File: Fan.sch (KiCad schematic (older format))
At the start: 9 parts, among them Q2 MOSFET_N, Q3 MOSFET_N, Q4 MOSFET_N, U11 OPA4170, U8 MCP4922-E/P

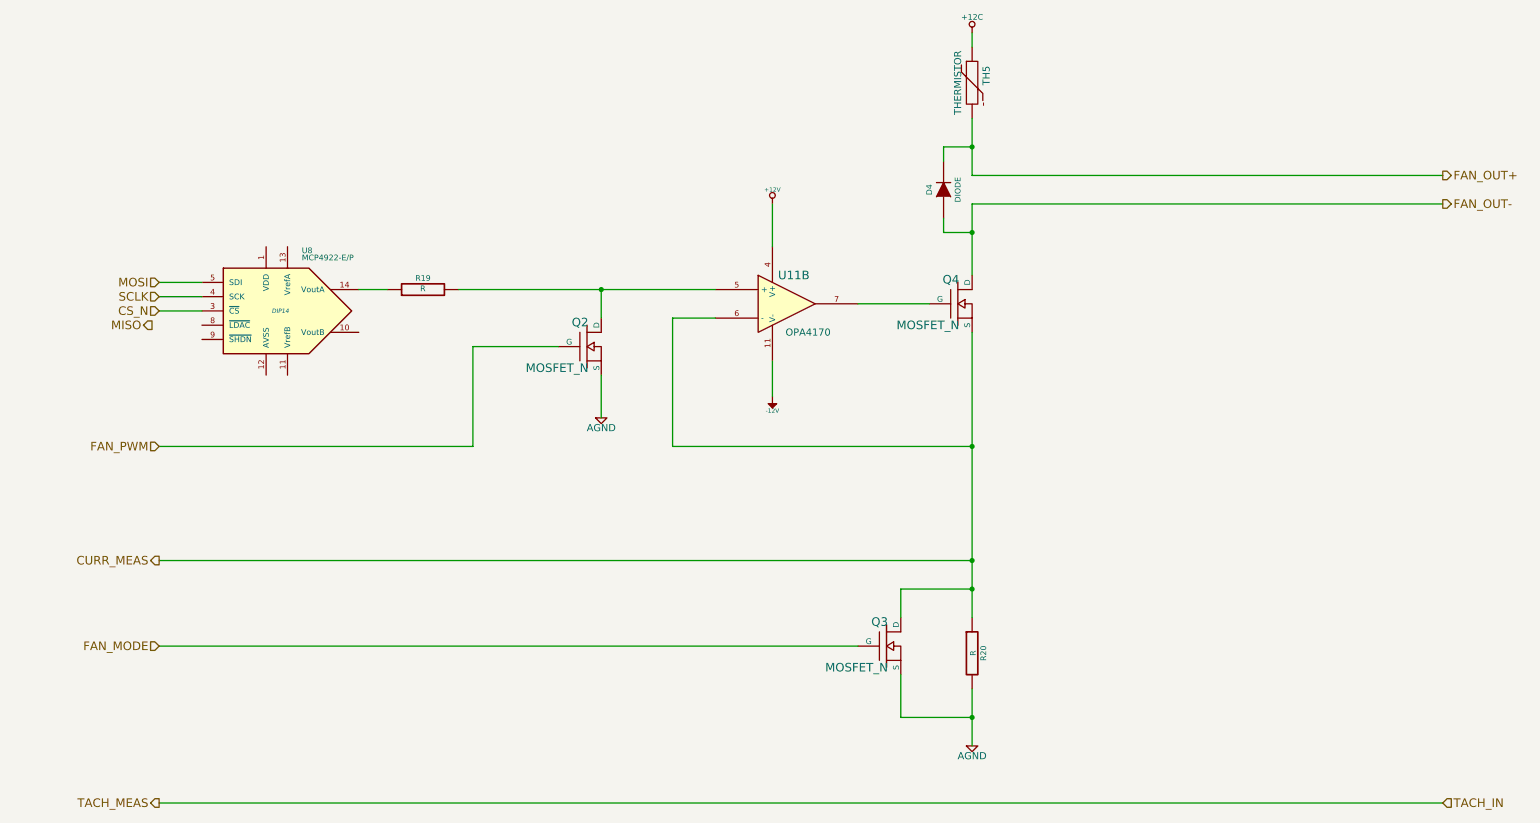
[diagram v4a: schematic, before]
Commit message: Associated and placed the Current/Fan Driver Module
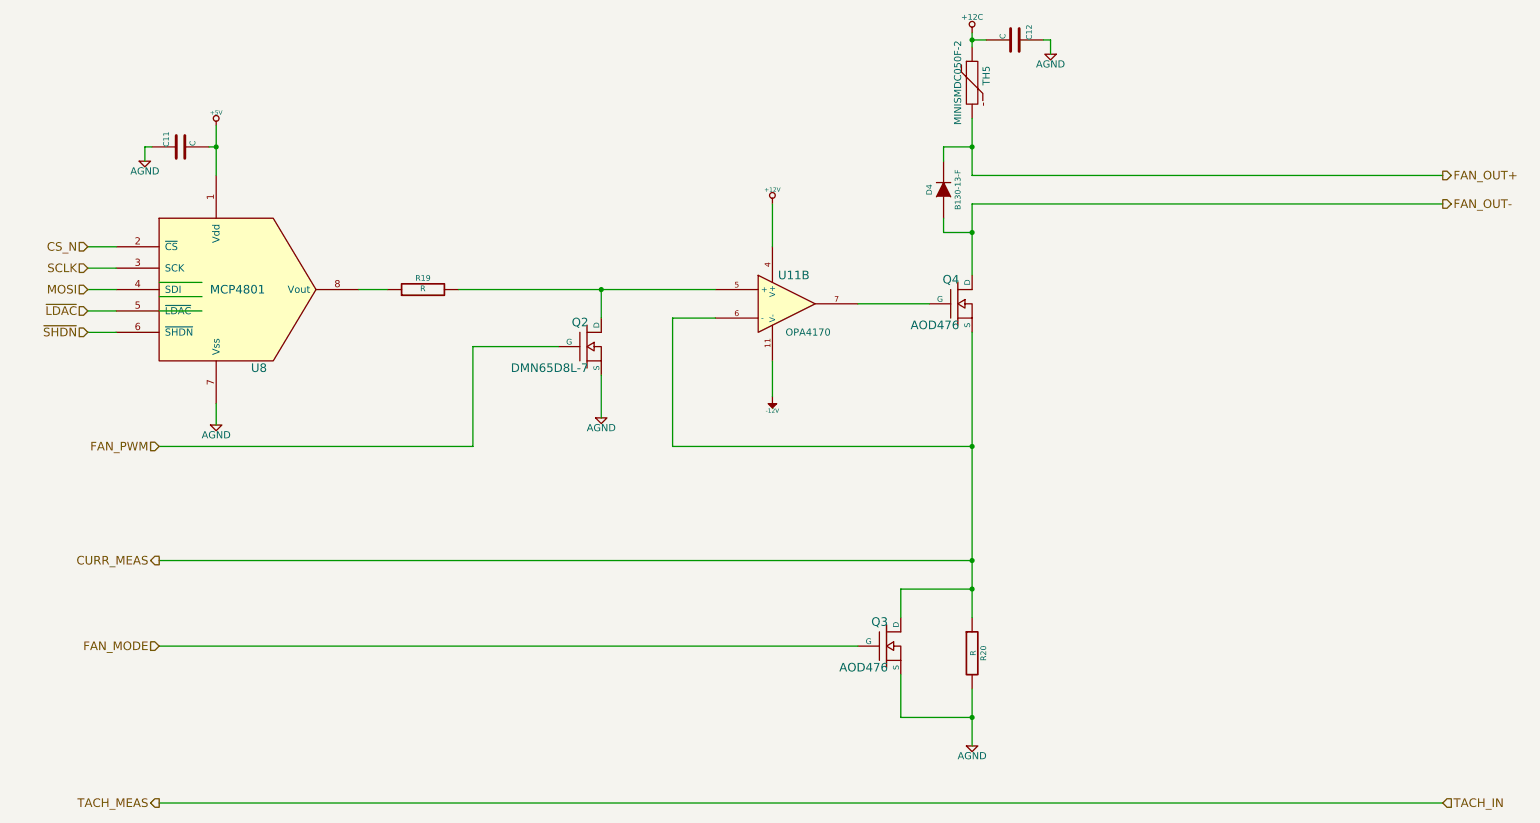
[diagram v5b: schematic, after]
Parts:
- removed Q2, Q3, Q4: MOSFET_N, symbol MOSFET_N
- removed U8: MCP4922-E/P, DIP14, symbol MCP4922-E/P
- added C11, C12: C, symbol C
- added Q2: DMN65D8L-7, symbol MOSFET_N_NUM
- added Q3, Q4: AOD476, symbol MOSFET_N_NUM
- added U8: MCP4801, symbol MCP4801
- D4: value DIODE -> B130-13-F; MFG Name (none) -> Diodes Inc; MFG Part Number (none) -> B130-13-F
- TH5: value THERMISTOR -> MINISMDC050F-2; MFG Name (none) -> TE; MFG Part Number (none) -> MINISMDC050F-2
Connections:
- net labels added: +5V, ~LDAC, ~SHDN
- net labels removed: MISO
- wire segments 34 -> 47
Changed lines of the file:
@@
-$EndComp
-$Comp
-L MOSFET_N Q4
-U 1 1 52F026F4
-P 7100 2600
-F 0 "Q4" H 7110 2770 60  0000 R CNN
-F 1 "MOSFET_N" H 7110 2450 60  0000 R CNN
-F 2 "" H 7100 2600 60  0000 C CNN
-F 3 "" H 7100 2600 60  0000 C CNN
-	1    7100 2600
-	1    0    0    -1
 $EndComp
 $Comp
@@
 $EndComp
 $Comp
-L AGND #PWR42
+L AGND #PWR45
 U 1 1 52F02747
 P 7200 5700
-F 0 "#PWR42" H 7200 5700 40  0001 C CNN
+F 0 "#PWR45" H 7200 5700 40  0001 C CNN
 F 1 "AGND" H 7200 5630 50  0000 C CNN
 F 2 "" H 7200 5700 60  0000 C CNN
@@
 $EndComp
 $Comp
-L +12V #PWR39
+L +12V #PWR42
 U 1 1 52F02768
 P 5800 1900
-F 0 "#PWR39" H 5800 1850 20  0001 C CNN
+F 0 "#PWR42" H 5800 1850 20  0001 C CNN
 F 1 "+12V" H 5800 2000 30  0000 C CNN
 F 2 "" H 5800 1900 60  0000 C CNN
@@
 $EndComp
 $Comp
-L -12V #PWR40
+L -12V #PWR43
 U 1 1 52F02786
 P 5800 3250
-F 0 "#PWR40" H 5800 3380 20  0001 C CNN
+F 0 "#PWR43" H 5800 3380 20  0001 C CNN
 F 1 "-12V" H 5800 3350 30  0000 C CNN
 F 2 "" H 5800 3250 60  0000 C CNN
@@
 $EndComp
 $Comp
-L AGND #PWR38
+L AGND #PWR41
 U 1 1 52F0282F
 P 4600 3400
-F 0 "#PWR38" H 4600 3400 40  0001 C CNN
+F 0 "#PWR41" H 4600 3400 40  0001 C CNN
 F 1 "AGND" H 4600 3330 50  0000 C CNN
 F 2 "" H 4600 3400 60  0000 C CNN
 F 3 "" H 4600 3400 60  0000 C CNN
 	1    4600 3400
-	1    0    0    -1
-$EndComp
-$Comp
-L MCP4922-E/P U8
-U 1 1 52F0284E
-P 2350 2650
-F 0 "U8" H 2500 3050 40  0000 L BNN
-F 1 "MCP4922-E/P" H 2500 3000 40  0000 L BNN
-F 2 "DIP14" H 2350 2650 30  0000 C CIN
-F 3 "" H 2350 2650 60  0000 C CNN
-	1    2350 2650
 	1    0    0    -1
 $EndComp
@@
 	0    -1   -1   0
 $EndComp
-Text HLabel 1500 2450 0    60   Input ~ 0
+Text HLabel 1000 2500 0    60   Input ~ 0
 MOSI
-Text HLabel 1450 2750 0    60   Output ~ 0
-MISO
-Text HLabel 1500 2650 0    60   Input ~ 0
+Text HLabel 1000 2200 0    60   Input ~ 0
 CS_N
-Text HLabel 1500 2550 0    60   Input ~ 0
+Text HLabel 1000 2350 0    60   Input ~ 0
 SCLK
-$Comp
-L MOSFET_N Q3
-U 1 1 52FBE00D
-P 6600 5000
-F 0 "Q3" H 6610 5170 60  0000 R CNN
-F 1 "MOSFET_N" H 6610 4850 60  0000 R CNN
-F 2 "" H 6600 5000 60  0000 C CNN
-F 3 "" H 6600 5000 60  0000 C CNN
-	1    6600 5000
-	1    0    0    -1
-$EndComp
 $Comp
 L THERMISTOR TH5
@@
 P 7200 1050
 F 0 "TH5" V 7300 1100 50  0000 C CNN
-F 1 "THERMISTOR" V 7100 1050 50  0000 C CNN
+F 1 "MINISMDC050F-2" V 7100 1050 50  0000 C CNN
 F 2 "" H 7200 1050 60  0000 C CNN
 F 3 "" H 7200 1050 60  0000 C CNN
+F 4 "TE" H 7200 1050 60  0001 C CNN "MFG Name"
+F 5 "MINISMDC050F-2" H 7200 1050 60  0001 C CNN "MFG Part Number"
 	1    7200 1050
 	1    0    0    -1
@@
 P 7000 1800
 F 0 "D4" H 7000 1900 40  0000 C CNN
-F 1 "DIODE" H 7000 1700 40  0000 C CNN
+F 1 "B130-13-F" H 7000 1700 40  0000 C CNN
 F 2 "" H 7000 1800 60  0000 C CNN
 F 3 "" H 7000 1800 60  0000 C CNN
+F 4 "Diodes Inc" H 7000 1800 60  0001 C CNN "MFG Name"
+F 5 "B130-13-F" H 7000 1800 60  0001 C CNN "MFG Part Number"
 	1    7000 1800
 	0    -1   -1   0
@@
 Wire Wire Line
 	10500 6100 1500 6100
-$Comp
-L MOSFET_N Q2
-U 1 1 52FBE558
-P 4500 2900
-F 0 "Q2" H 4510 3070 60  0000 R CNN
-F 1 "MOSFET_N" H 4510 2750 60  0000 R CNN
-F 2 "" H 4500 2900 60  0000 C CNN
-F 3 "" H 4500 2900 60  0000 C CNN
-	1    4500 2900
-	1    0    0    -1
-$EndComp
 Wire Wire Line
 	4600 2700 4600 2500
@@
 	1500 5000 6400 5000
 $Comp
-L +12C #PWR41
+L +12C #PWR44
 U 1 1 52FBEABF
 P 7200 700
-F 0 "#PWR41" H 7200 670 30  0001 C CNN
+F 0 "#PWR44" H 7200 670 30  0001 C CNN
 F 1 "+12C" H 7200 810 40  0000 C CNN
 F 2 "" H 7200 700 60  0000 C CNN
@@
 	1    0    0    -1
 $EndComp
+$Comp
+L MCP4801 U8
+U 1 1 53090AC6
+P 1900 2500
+F 0 "U8" H 2200 1950 60  0000 C CNN
+F 1 "MCP4801" H 2050 2500 60  0000 C CNN
+F 2 "" H 1900 2500 60  0000 C CNN
+F 3 "" H 1900 2500 60  0000 C CNN
+	1    1900 2500
+	1    0    0    -1
+$EndComp
+Wire Wire Line
+	1000 2200 1200 2200
+Wire Wire Line
+	1000 2350 1200 2350
+Wire Wire Line
+	1000 2500 1200 2500
+Text HLabel 1000 2650 0    60   Input ~ 0
+~LDAC
+Text HLabel 1000 2800 0    60   Input ~ 0
+~SHDN
+Wire Wire Line
+	1000 2650 1200 2650
+Wire Wire Line
+	1000 2800 1200 2800
+$Comp
+L +5V #PWR39
+U 1 1 530AC1D4
+P 1900 1350
+F 0 "#PWR39" H 1900 1440 20  0001 C CNN
+F 1 "+5V" H 1900 1440 30  0000 C CNN
+F 2 "" H 1900 1350 60  0000 C CNN
+F 3 "" H 1900 1350 60  0000 C CNN
+	1    1900 1350
+	-1   0    0    -1
+$EndComp
+$Comp
+L C C11
+U 1 1 530AC1DA
+P 1650 1500
+F 0 "C11" H 1650 1600 40  0000 L CNN
+F 1 "C" H 1656 1415 40  0000 L CNN
+F 2 "" H 1688 1350 30  0000 C CNN
+F 3 "" H 1650 1500 60  0000 C CNN
+	1    1650 1500
+	0    -1   -1   0
+$EndComp
+$Comp
+L AGND #PWR38
+U 1 1 530AC1E0
+P 1400 1600
+F 0 "#PWR38" H 1400 1600 40  0001 C CNN
+F 1 "AGND" H 1400 1530 50  0000 C CNN
+F 2 "" H 1400 1600 60  0000 C CNN
+F 3 "" H 1400 1600 60  0000 C CNN
+	1    1400 1600
+	1    0    0    -1
+$EndComp
+Wire Wire Line
+	1450 1500 1400 1500
+Connection ~ 1900 1500
+Wire Wire Line
+	1850 1500 1900 1500
+Wire Wire Line
+	1400 1500 1400 1600
+Wire Wire Line
+	1900 1350 1900 1700
+$Comp
+L AGND #PWR40
+U 1 1 530AC1EB
+P 1900 3450
+F 0 "#PWR40" H 1900 3450 40  0001 C CNN
+F 1 "AGND" H 1900 3380 50  0000 C CNN
+F 2 "" H 1900 3450 60  0000 C CNN
+F 3 "" H 1900 3450 60  0000 C CNN
+	1    1900 3450
+	1    0    0    -1
+$EndComp
+Wire Wire Line
+	1900 3450 1900 3300
+$Comp
+L C C12
+U 1 1 530AD561
+P 7500 750
+F 0 "C12" H 7500 850 40  0000 L CNN
+F 1 "C" H 7506 665 40  0000 L CNN
+F 2 "" H 7538 600 30  0000 C CNN
+F 3 "" H 7500 750 60  0000 C CNN
+	1    7500 750
+	0    1    -1   0
+$EndComp
+$Comp
+L AGND #PWR46
+U 1 1 530AD567
+P 7750 850
+F 0 "#PWR46" H 7750 850 40  0001 C CNN
+F 1 "AGND" H 7750 780 50  0000 C CNN
+F 2 "" H 7750 850 60  0000 C CNN
+F 3 "" H 7750 850 60  0000 C CNN
+	1    7750 850
+	-1   0    0    -1
+$EndComp
+Wire Wire Line
+	7700 750  7750 750
+Wire Wire Line
+	7750 750  7750 850
+Wire Wire Line
+	7300 750  7200 750
+Connection ~ 7200 750
+$Comp
+L MOSFET_N_NUM Q4
+U 1 1 53091D11
+P 7100 2600
+F 0 "Q4" H 7110 2770 60  0000 R CNN
+F 1 "AOD476" H 7110 2450 60  0000 R CNN
+F 2 "" H 7100 2600 60  0000 C CNN
+F 3 "" H 7100 2600 60  0000 C CNN
+F 4 "Alpha and Omega" H 7100 2600 60  0001 C CNN "MFG Name"
+F 5 "AOD476" H 7100 2600 60  0001 C CNN "MFG Part Number"
+	1    7100 2600
+	1    0    0    -1
+$EndComp
+$Comp
+L MOSFET_N_NUM Q3
+U 1 1 53091DDF
+P 6600 5000
+F 0 "Q3" H 6610 5170 60  0000 R CNN
+F 1 "AOD476" H 6610 4850 60  0000 R CNN
+F 2 "" H 6600 5000 60  0000 C CNN
+F 3 "" H 6600 5000 60  0000 C CNN
+F 4 "Alpha and Omega" H 6600 5000 60  0001 C CNN "MFG Name"
+F 5 "AOD476" H 6600 5000 60  0001 C CNN "MFG Part Number"
+	1    6600 5000
+	1    0    0    -1
+$EndComp
+$Comp
+L MOSFET_N_NUM Q2
+U 1 1 53091E18
+P 4500 2900
+F 0 "Q2" H 4510 3070 60  0000 R CNN
+F 1 "DMN65D8L-7" H 4510 2750 60  0000 R CNN
+F 2 "" H 4500 2900 60  0000 C CNN
+F 3 "" H 4500 2900 60  0000 C CNN
+F 4 "Diodes Inc" H 4500 2900 60  0001 C CNN "MFG Name"
+F 5 "DMN65D8L-7" H 4500 2900 60  0001 C CNN "MFG Part Number"
+	1    4500 2900
+	1    0    0    -1
+$EndComp

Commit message: Associated and placed the Power Filter Module
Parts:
- TH5: MFG Name TE -> TE Connectivity
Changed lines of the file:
@@
 $EndComp
 $Comp
-L AGND #PWR45
+L AGND #PWR48
 U 1 1 52F02747
 P 7200 5700
-F 0 "#PWR45" H 7200 5700 40  0001 C CNN
+F 0 "#PWR48" H 7200 5700 40  0001 C CNN
 F 1 "AGND" H 7200 5630 50  0000 C CNN
 F 2 "" H 7200 5700 60  0000 C CNN
@@
 $EndComp
 $Comp
-L +12V #PWR42
+L +12V #PWR45
 U 1 1 52F02768
 P 5800 1900
-F 0 "#PWR42" H 5800 1850 20  0001 C CNN
+F 0 "#PWR45" H 5800 1850 20  0001 C CNN
 F 1 "+12V" H 5800 2000 30  0000 C CNN
 F 2 "" H 5800 1900 60  0000 C CNN
@@
 $EndComp
 $Comp
-L -12V #PWR43
+L -12V #PWR46
 U 1 1 52F02786
 P 5800 3250
-F 0 "#PWR43" H 5800 3380 20  0001 C CNN
+F 0 "#PWR46" H 5800 3380 20  0001 C CNN
 F 1 "-12V" H 5800 3350 30  0000 C CNN
 F 2 "" H 5800 3250 60  0000 C CNN
@@
 $EndComp
 $Comp
-L AGND #PWR41
+L AGND #PWR44
 U 1 1 52F0282F
 P 4600 3400
-F 0 "#PWR41" H 4600 3400 40  0001 C CNN
+F 0 "#PWR44" H 4600 3400 40  0001 C CNN
 F 1 "AGND" H 4600 3330 50  0000 C CNN
 F 2 "" H 4600 3400 60  0000 C CNN
@@
 F 2 "" H 7200 1050 60  0000 C CNN
 F 3 "" H 7200 1050 60  0000 C CNN
-F 4 "TE" H 7200 1050 60  0001 C CNN "MFG Name"
+F 4 "TE Connectivity" H 7200 1050 60  0001 C CNN "MFG Name"
 F 5 "MINISMDC050F-2" H 7200 1050 60  0001 C CNN "MFG Part Number"
 	1    7200 1050
@@
 	1500 5000 6400 5000
 $Comp
-L +12C #PWR44
+L +12C #PWR47
 U 1 1 52FBEABF
 P 7200 700
-F 0 "#PWR44" H 7200 670 30  0001 C CNN
+F 0 "#PWR47" H 7200 670 30  0001 C CNN
 F 1 "+12C" H 7200 810 40  0000 C CNN
 F 2 "" H 7200 700 60  0000 C CNN
@@
 	1000 2800 1200 2800
 $Comp
-L +5V #PWR39
+L +5V #PWR42
 U 1 1 530AC1D4
 P 1900 1350
-F 0 "#PWR39" H 1900 1440 20  0001 C CNN
+F 0 "#PWR42" H 1900 1440 20  0001 C CNN
 F 1 "+5V" H 1900 1440 30  0000 C CNN
 F 2 "" H 1900 1350 60  0000 C CNN
@@
 $EndComp
 $Comp
-L AGND #PWR38
+L AGND #PWR41
 U 1 1 530AC1E0
 P 1400 1600
-F 0 "#PWR38" H 1400 1600 40  0001 C CNN
+F 0 "#PWR41" H 1400 1600 40  0001 C CNN
 F 1 "AGND" H 1400 1530 50  0000 C CNN
 F 2 "" H 1400 1600 60  0000 C CNN
@@
 	1900 1350 1900 1700
 $Comp
-L AGND #PWR40
+L AGND #PWR43
 U 1 1 530AC1EB
 P 1900 3450
-F 0 "#PWR40" H 1900 3450 40  0001 C CNN
+F 0 "#PWR43" H 1900 3450 40  0001 C CNN
 F 1 "AGND" H 1900 3380 50  0000 C CNN
 F 2 "" H 1900 3450 60  0000 C CNN
@@
 $EndComp
 $Comp
-L AGND #PWR46
+L AGND #PWR49
 U 1 1 530AD567
 P 7750 850
-F 0 "#PWR46" H 7750 850 40  0001 C CNN
+F 0 "#PWR49" H 7750 850 40  0001 C CNN
 F 1 "AGND" H 7750 780 50  0000 C CNN
 F 2 "" H 7750 850 60  0000 C CNN
